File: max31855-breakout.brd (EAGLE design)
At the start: 25 x 25 mm, 6 parts

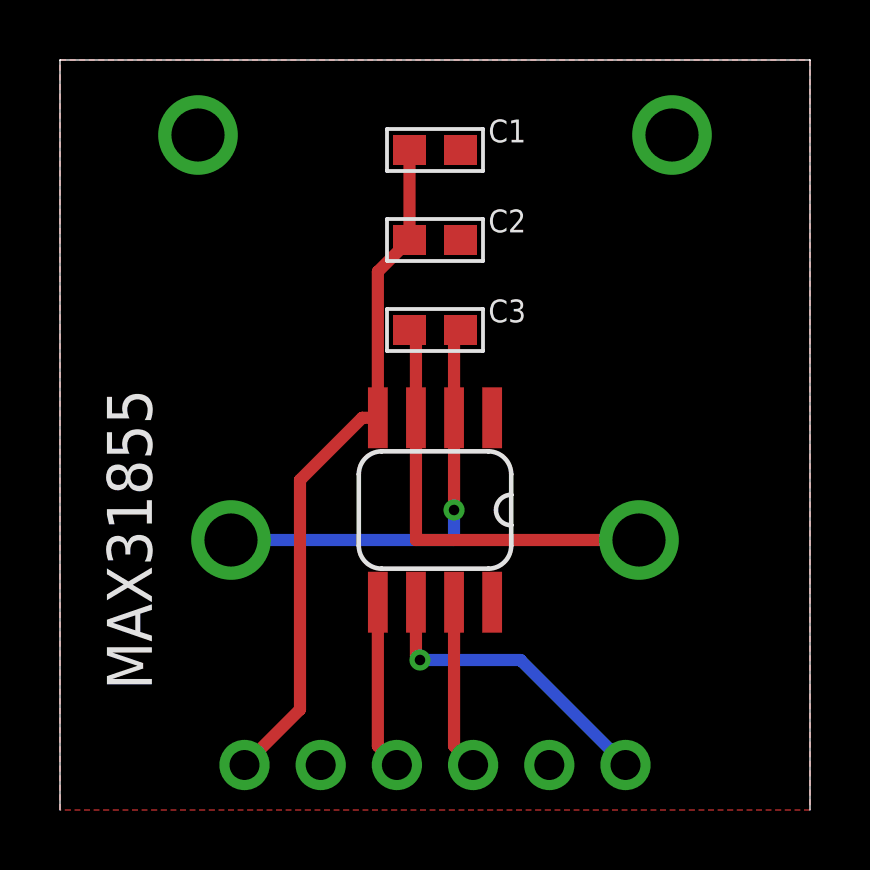
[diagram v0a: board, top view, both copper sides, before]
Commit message: chamfer, label, add resistor jumper for use with xmega breakout - design confirmed working.
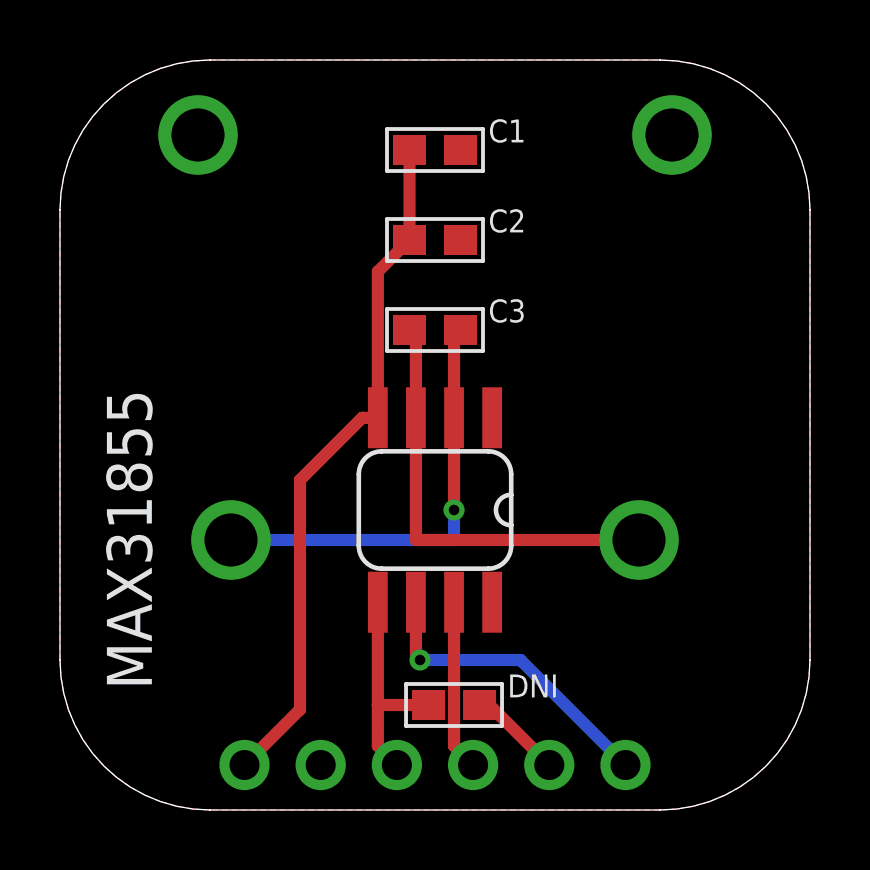
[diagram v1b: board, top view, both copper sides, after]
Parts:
- added DNI: DNI, nonolith:0603
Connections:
- net SCK: now also DNI.1
- net SI: now also DNI.2
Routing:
- net SI: track 0.00 -> 3.15 mm
- net SCK: track 5.69 -> 7.38 mm
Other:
- outline, holes or cut-outs redrawn
- board text added: "3v3"
- board text added: "CS"
- board text added: "DNC"
- board text added: "GND"
- board text added: "SCK"
- board text added: "SO"
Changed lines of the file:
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@@
 <?xml version="1.0" encoding="utf-8"?>
 <!DOCTYPE eagle SYSTEM "eagle.dtd">
-<eagle version="6.3">
+<eagle version="6.4">
 <drawing>
 <settings>
@@
 <board>
 <plain>
-<wire x1="25" y1="0" x2="25" y2="25" width="0" layer="20"/>
-<wire x1="25" y1="25" x2="0" y2="25" width="0" layer="20"/>
-<wire x1="0" y1="25" x2="0" y2="0" width="0" layer="20"/>
+<wire x1="0" y1="20" x2="0" y2="5" width="0" layer="20"/>
+<wire x1="0" y1="5" x2="5" y2="0" width="0" layer="20" curve="90"/>
+<wire x1="5" y1="0" x2="20" y2="0" width="0" layer="20"/>
+<wire x1="20" y1="0" x2="25" y2="5" width="0" layer="20" curve="90"/>
+<wire x1="25" y1="5" x2="25" y2="20" width="0" layer="20"/>
+<wire x1="25" y1="20" x2="20" y2="25" width="0" layer="20" curve="90"/>
+<wire x1="20" y1="25" x2="5" y2="25" width="0" layer="20"/>
+<wire x1="5" y1="25" x2="0" y2="20" width="0" layer="20" curve="90"/>
+<text x="6" y="3" size="1" layer="28" font="vector" ratio="12" rot="MR90">3v3</text>
+<text x="8" y="3" size="1" layer="28" font="vector" ratio="12" rot="MR90">GND</text>
+<text x="11" y="3" size="1" layer="28" font="vector" ratio="12" rot="MR90">SCK</text>
+<text x="13" y="3" size="1" layer="28" font="vector" ratio="12" rot="MR90">SO</text>
+<text x="16" y="3" size="1" layer="28" font="vector" ratio="12" rot="MR90">DNC</text>
+<text x="18.5" y="3" size="1" layer="28" font="vector" ratio="12" rot="MR90">CS</text>
 </plain>
 <attributes>
@@
 <attribute name="VALUE" x="4.88" y="-1.675" size="1.27" layer="27"/>
 </element>
+<element name="DNI" library="nonolith" package="0603" value="DNI" x="13.135" y="3.5"/>
 </elements>
 <signals>
@@
 <contactref element="U$1" pad="1"/>
 <polygon width="0.254" layer="1">
-<vertex x="0" y="25"/>
-<vertex x="25" y="25"/>
-<vertex x="25" y="0"/>
-<vertex x="0" y="0"/>
+<vertex x="20" y="0"/>
+<vertex x="5" y="0" curve="-90"/>
+<vertex x="0" y="5"/>
+<vertex x="0" y="20" curve="-90"/>
+<vertex x="5" y="25"/>
+<vertex x="20" y="25" curve="-90"/>
+<vertex x="25" y="20"/>
+<vertex x="25" y="5" curve="-90"/>
 </polygon>
 <contactref element="U$2" pad="GND@4"/>
@@
 <contactref element="U$1" pad="5"/>
 <contactref element="JP1" pad="3"/>
-<wire x1="10.595" y1="2.135" x2="10.595" y2="6.9266" width="0.4064" layer="1"/>
+<wire x1="10.595" y1="2.135" x2="10.595" y2="3" width="0.4064" layer="1"/>
+<wire x1="10.595" y1="3.5" x2="10.595" y2="6.9266" width="0.4064" layer="1"/>
 <wire x1="10.595" y1="2.135" x2="11.23" y2="1.5" width="0.4064" layer="1"/>
+<contactref element="DNI" pad="1"/>
+<wire x1="12.285" y1="3.5" x2="10.595" y2="3.5" width="0.4064" layer="1"/>
+<wire x1="10.595" y1="3.5" x2="10.595" y2="3" width="0.4064" layer="1"/>
 </signal>
 <signal name="CS">
@@
 <signal name="SI">
 <contactref element="JP1" pad="5"/>
+<contactref element="DNI" pad="2"/>
+<wire x1="13.985" y1="3.5" x2="14.31" y2="3.5" width="0.4064" layer="1"/>
+<wire x1="14.31" y1="3.5" x2="16.31" y2="1.5" width="0.4064" layer="1"/>
 </signal>
 </signals>
